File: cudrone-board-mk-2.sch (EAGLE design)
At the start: 1 part, among them U1 EDISON_CONNECTOR_FULLSOCKET

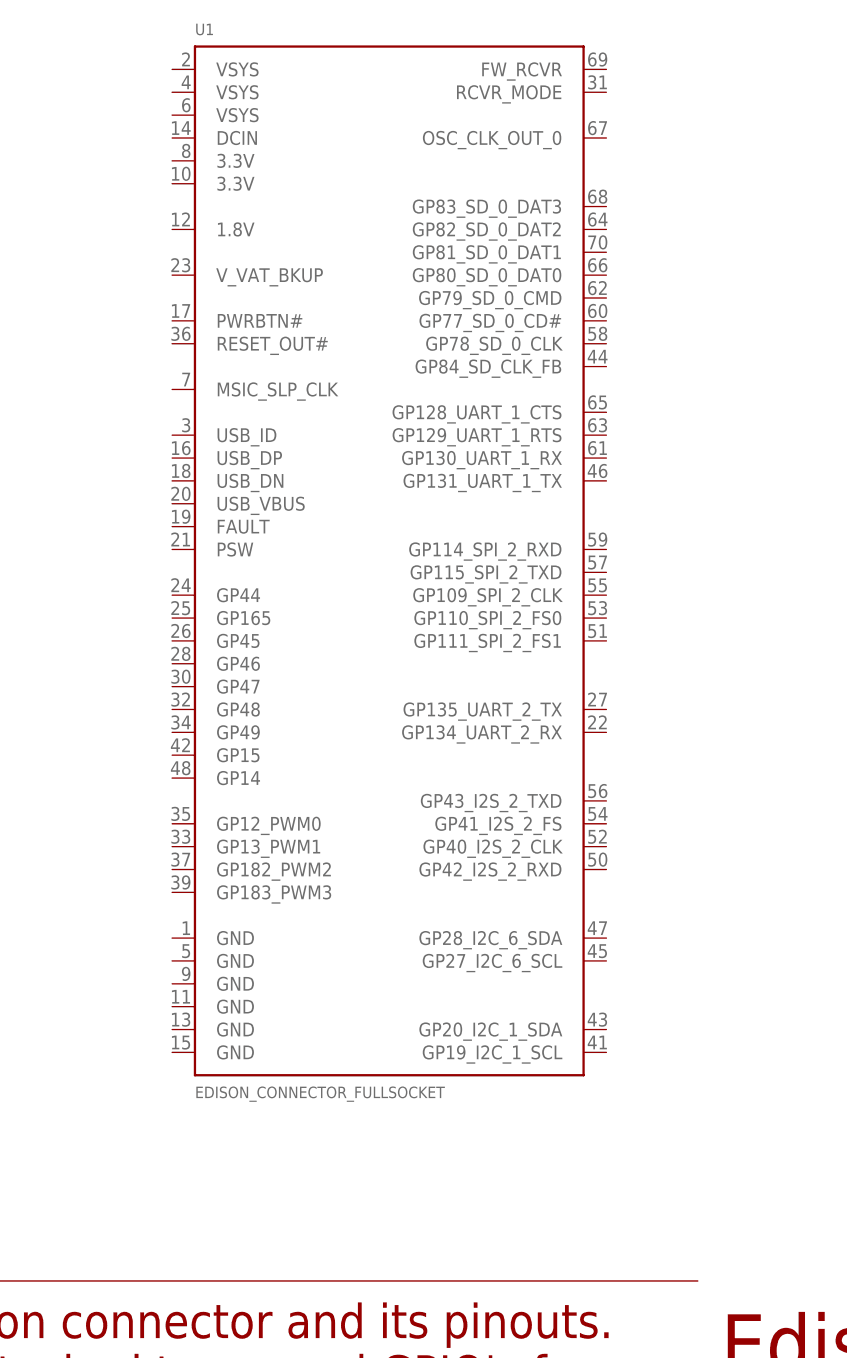
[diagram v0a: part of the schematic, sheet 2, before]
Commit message: Added several libraries
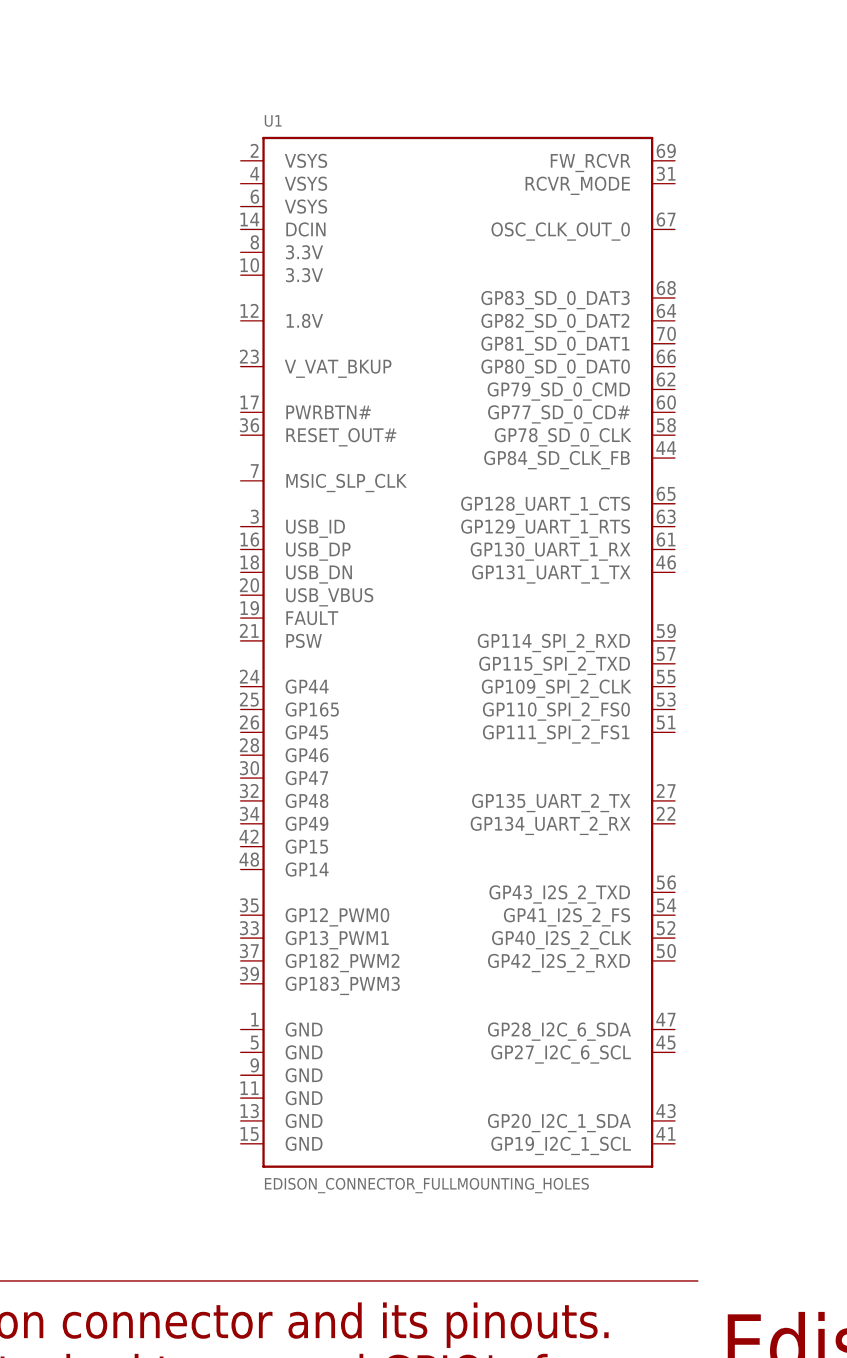
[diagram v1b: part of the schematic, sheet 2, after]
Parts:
- U1: value EDISON_CONNECTOR_FULLSOCKET -> EDISON_CONNECTOR_FULLMOUNTING_HOLES; device SparkFun-Boards:EDISON_CONNECTOR_FULLSOCKET -> SparkFun-Boards:EDISON_CONNECTOR_FULLMOUNTING_HOLES
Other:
- moved on the sheet: U1
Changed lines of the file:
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@@
 </classes>
 <parts>
-<part name="U1" library="SparkFun-Boards" deviceset="EDISON_CONNECTOR_FULL" device="SOCKET"/>
 <part name="FRAME1" library="frames" deviceset="LETTER_L" device=""/>
 <part name="FRAME2" library="frames" deviceset="LETTER_L" device=""/>
@@
 <part name="FRAME8" library="frames" deviceset="LETTER_L" device=""/>
 <part name="FRAME9" library="frames" deviceset="LETTER_L" device=""/>
+<part name="U1" library="SparkFun-Boards" deviceset="EDISON_CONNECTOR_FULL" device="MOUNTING_HOLES"/>
 </parts>
 <sheets>
@@
 </plain>
 <instances>
-<instance part="U1" gate="G$1" x="93.98" y="142.24"/>
 <instance part="FRAME1" gate="G$1" x="0" y="0"/>
 <instance part="FRAME1" gate="G$2" x="147.32" y="0"/>
+<instance part="U1" gate="G$1" x="101.6" y="132.08"/>
 </instances>
 <busses>

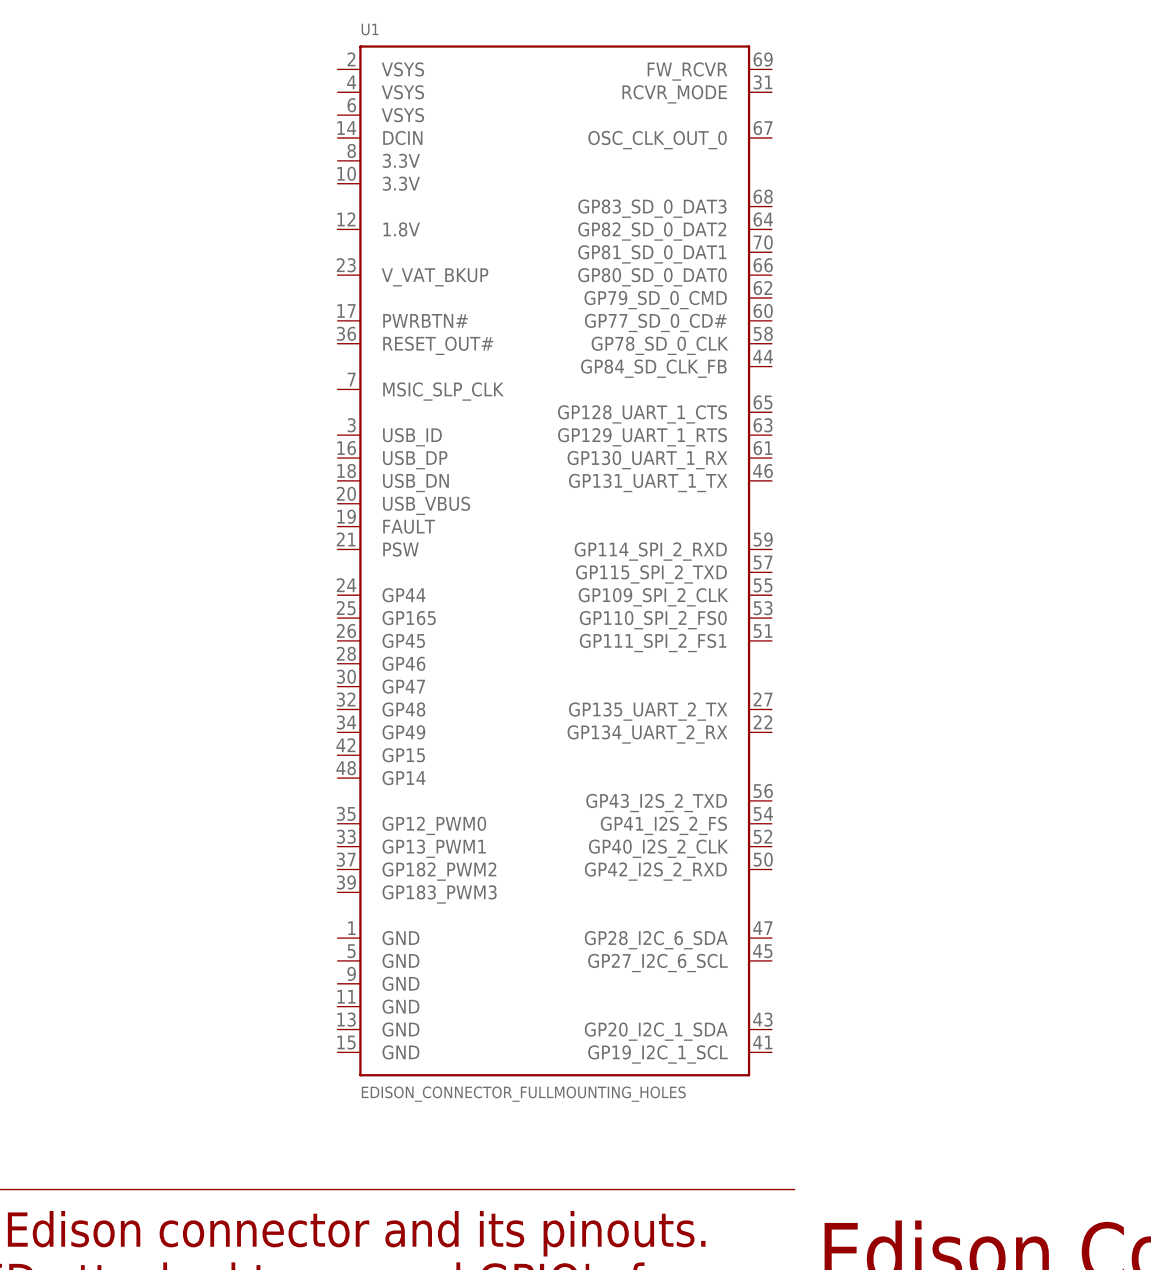
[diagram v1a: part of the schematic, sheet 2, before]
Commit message: Labeled edison nets and added RTC backup battery
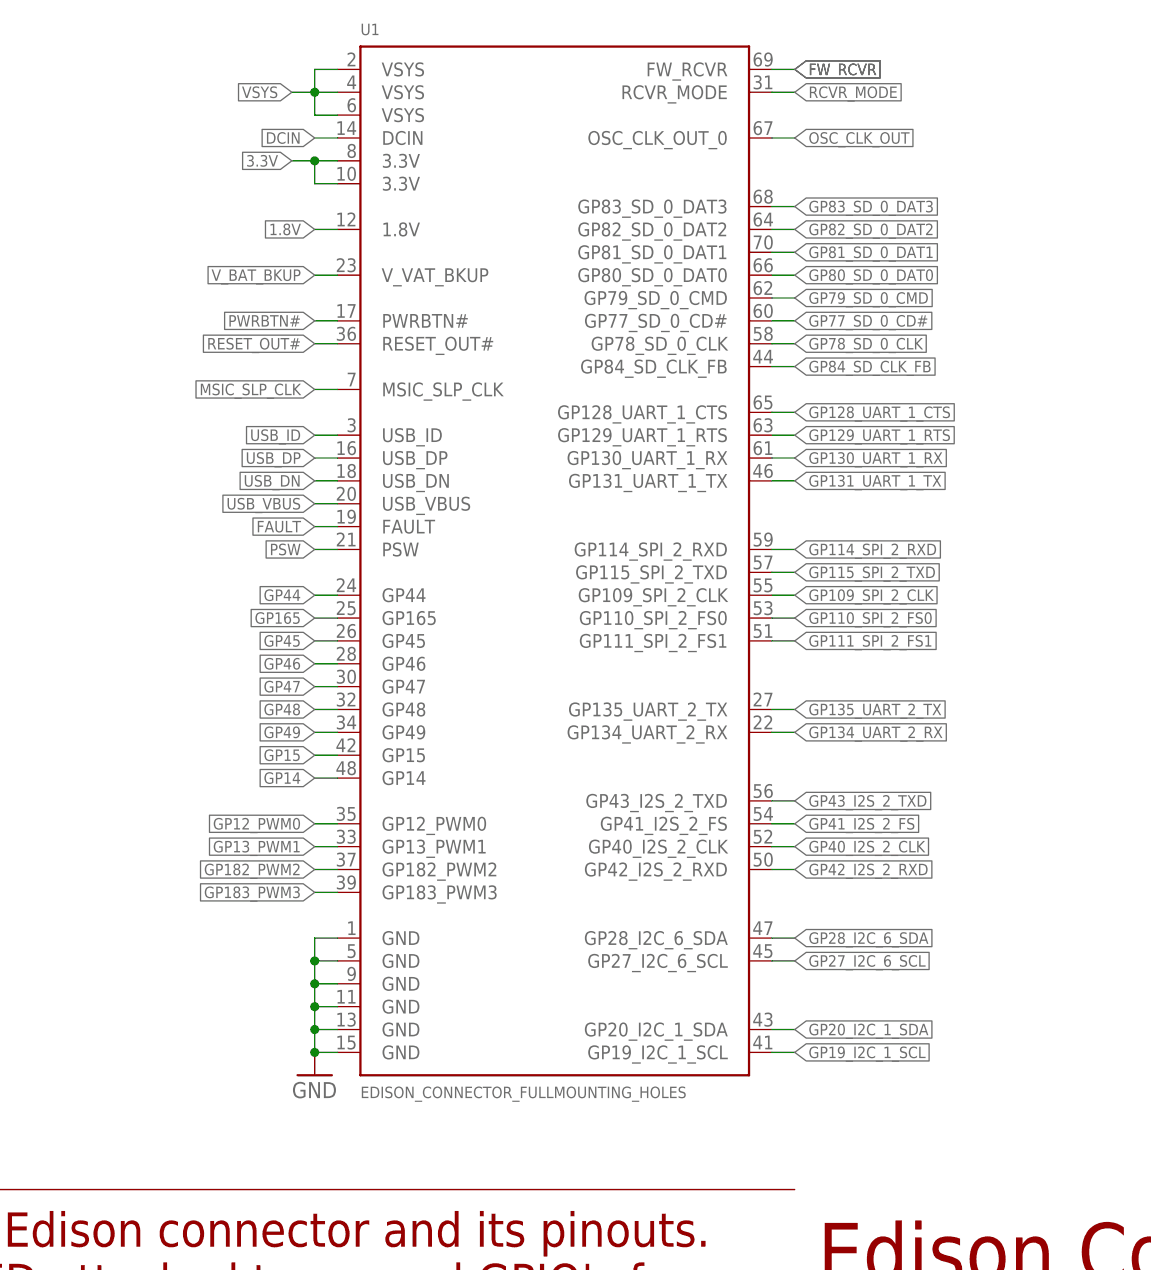
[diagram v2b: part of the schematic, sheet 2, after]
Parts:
- added BAT_BACKUP: RTC backup battery, SparkFun-Electromechanical:BATTERY12MM
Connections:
- new net 1.8V: U1.1.8V
- new net 3.3V: U1.3.3V@1, U1.3.3V@2
- new net DCIN: U1.DCIN
- new net FAULT: U1.FAULT
- new net FW_RCVR: U1.FW_RCVR
- new net GND: BAT_BACKUP.-, U1.GND@1, U1.GND@2, U1.GND@3, U1.GND@4, U1.GND@5, U1.GND@6
- new net GP109_SPI_2_CLK: U1.GP109_SPI_2_CLK
- new net GP110_SPI_2_FS0: U1.GP110_SPI_2_FS0
- new net GP111_SPI_2_FS1: U1.GP111_SPI_2_FS1
- new net GP114_SPI_2_RXD: U1.GP114_SPI_2_RXD
- new net GP115_SPI_2_TXD: U1.GP115_SPI_2_TXD
- new net GP128_UART_1_CTS: U1.GP128_UART_1_CTS
- new net GP129_UART_1_RTS: U1.GP129_UART_1_RTS
- new net GP12_PWM0: U1.GP12_PWM0
- new net GP130_UART_1_RX: U1.GP130_UART_1_RX
- new net GP131_UART_1_TX: U1.GP131_UART_1_TX
- new net GP134_UART_2_RX: U1.GP134_UART_2_RX
- new net GP135_UART_2_TX: U1.GP135_UART_2_TX
- new net GP13_PWM1: U1.GP13_PWM1
- new net GP14: U1.GP14
- new net GP15: U1.GP15
- new net GP165: U1.GP165
- new net GP182_PWM2: U1.GP182_PWM2
- new net GP183_PWM3: U1.GP183_PWM3
- new net GP19_I2C_1_SCL: U1.GP19_I2C_1_SCL
- new net GP20_I2C_1_SDA: U1.GP20_I2C_1_SDA
- new net GP27_I2C_6_SCL: U1.GP27_I2C_6_SCL
- new net GP28_I2C_6_SDA: U1.GP28_I2C_6_SDA
- new net GP40_I2S_2_CLK: U1.GP40_I2S_2_CLK
- new net GP41_I2S_2_FS: U1.GP41_I2S_2_FS
- new net GP42_I2S_2_RXD: U1.GP42_I2S_2_RXD
- new net GP43_I2S_2_TXD: U1.GP43_I2S_2_TXD
- new net GP44: U1.GP44
- new net GP45: U1.GP45
- new net GP46: U1.GP46
- new net GP47: U1.GP47
- new net GP48: U1.GP48
- new net GP49: U1.GP49
- new net GP77_SD_0_CD#: U1.GP77_SD_0_CD#
- new net GP78_SD_0_CLK: U1.GP78_SD_0_CLK
- new net GP79_SD_0_CMD: U1.GP79_SD_0_CMD
- new net GP80_SD_0_DAT0: U1.GP80_SD_0_DAT0
- new net GP81_SD_0_DAT1: U1.GP81_SD_0_DAT1
- new net GP82_SD_0_DAT2: U1.GP82_SD_0_DAT2
- new net GP83_SD_0_DAT3: U1.GP83_SD_0_DAT3
- new net GP84_SD_CLK_FB: U1.GP84_SD_CLK_FB
- new net MSIC_SLP_CLK: U1.MSIC_SLP_CLK
- new net OSC_CLK_OUT: U1.OSC_CLK_OUT_0
- new net PSW: U1.PSW
- new net PWRBTN#: U1.PWRBTN#
- new net RCVR_MODE: U1.RCVR_MODE
- new net RESET_OUT#: U1.RESET_OUT#
- new net USB_DN: U1.USB_DN
- new net USB_DP: U1.USB_DP
- new net USB_ID: U1.USB_ID
- new net USB_VBUS: U1.USB_VBUS
- new net VSYS: U1.VSYS@1, U1.VSYS@2, U1.VSYS@3
- new net V_BAT_BKUP: BAT_BACKUP.+, U1.V_VAT_BKUP
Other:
- note added: "Contains switching power regulator and RTC backup battery."
- note removed: "This sheet provides the power for main bus from esc power It contains a backup battery chargerwhich automatically kicks in the battery if the main power fails and signals the main controller so it can take action. It also contains nessisary regulators. There are also LED status lights. Contains power moniter which communicates via I2C"

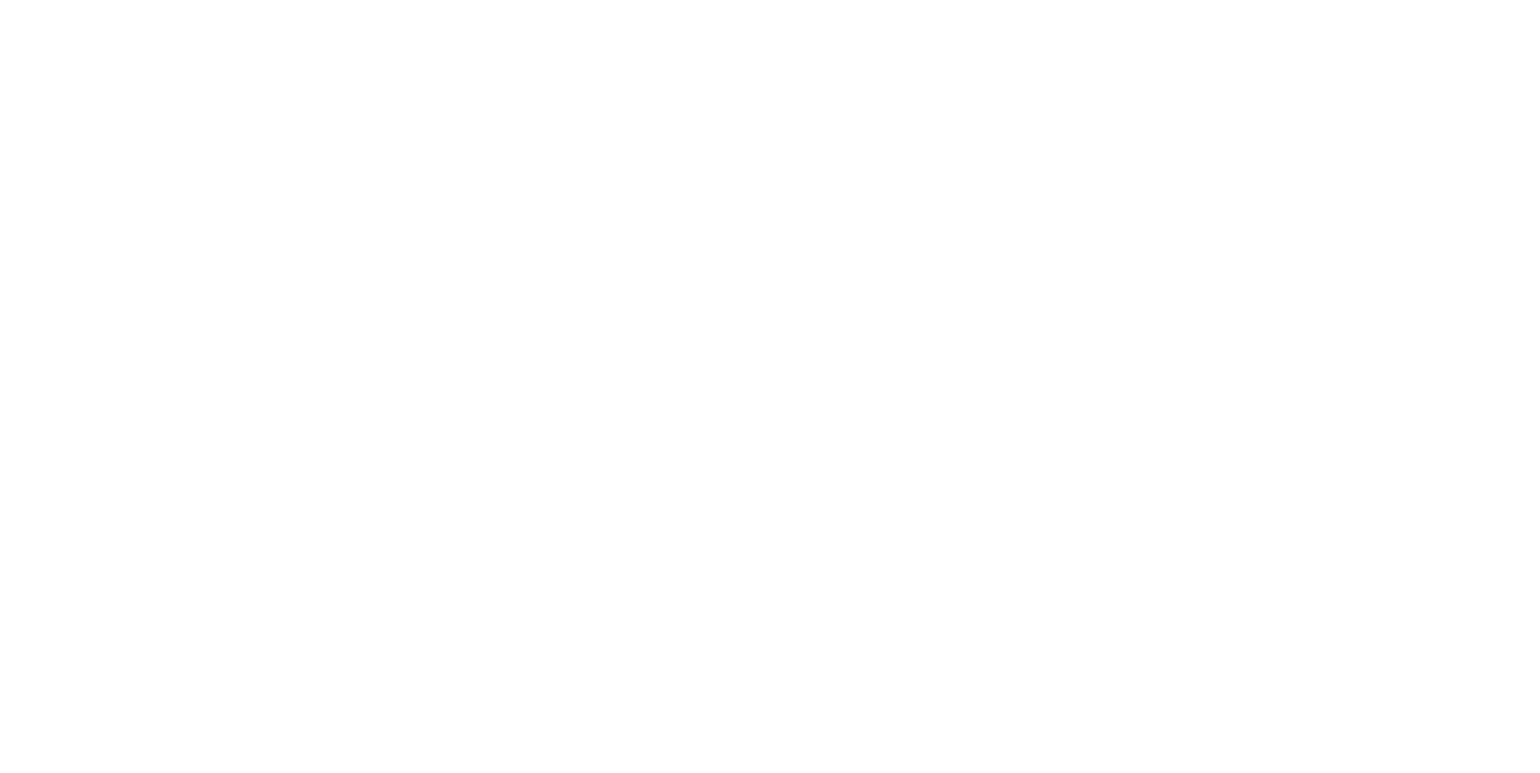
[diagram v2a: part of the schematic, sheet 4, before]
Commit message: Added contents of base block to schematic
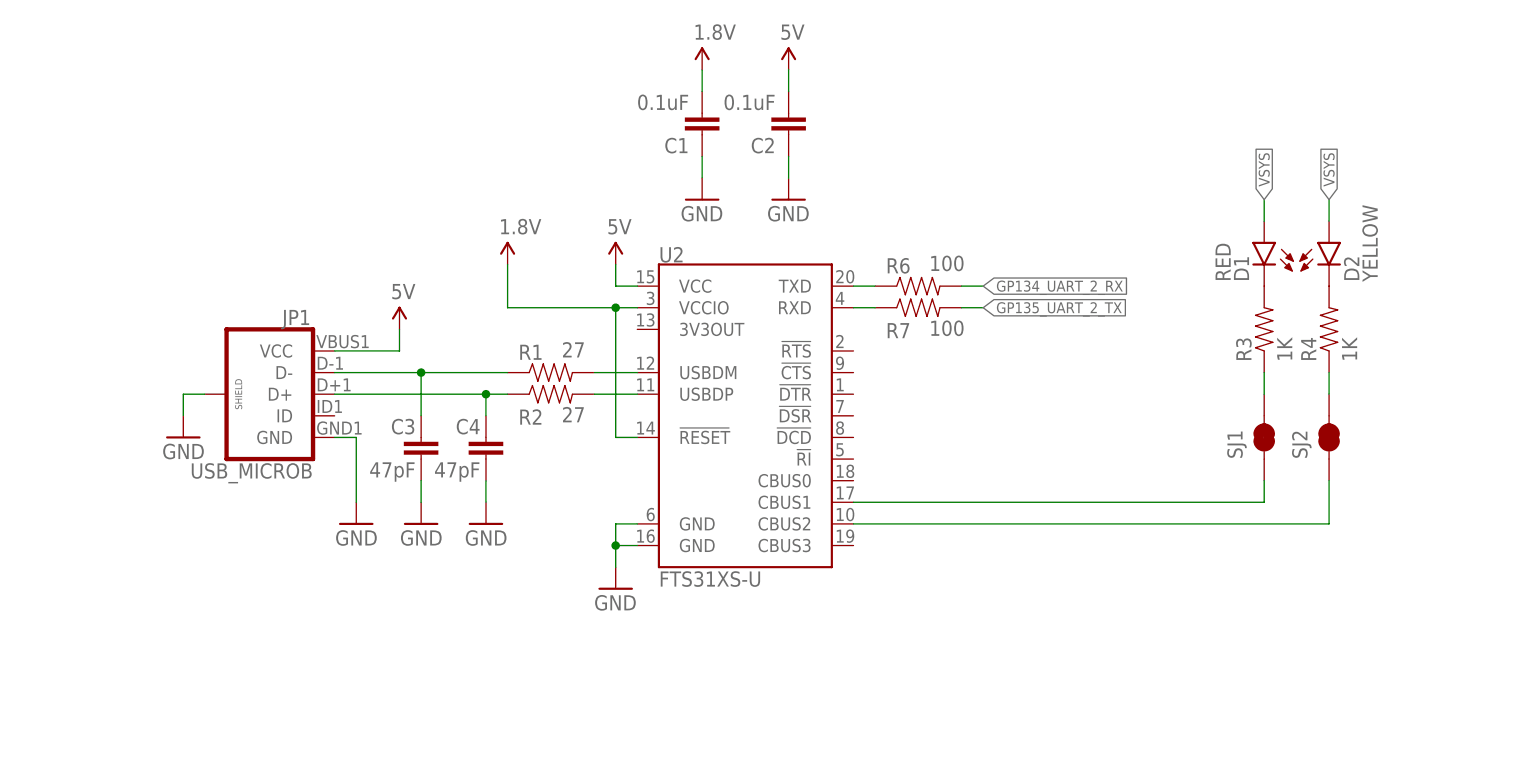
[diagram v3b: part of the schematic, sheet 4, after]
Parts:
- added C1, C2: 0.1uF, SparkFun-Capacitors:0.1UF-25V(+80/-20%)(0603)
- added C3, C4, C7: 47pF, SparkFun-Capacitors:47PF-50V-5%(0603)
- added C6, C9: 22uF, SparkFun-Capacitors:22UF-6.3V-20%(0805)
- added C8: 10uF, SparkFun-Capacitors:10UF-6.3V-20%(1206)
- added D1: RED, SparkFun-LED:LED-RED0603
- added D2: YELLOW, SparkFun-LED:LED-YELLOW0603
- added D3: BLUE, SparkFun-LED:LED-BLUE0603
- added D4: DIODE-SCHOTTKY-MBRA140, SparkFun-DiscreteSemi:DIODE-SCHOTTKY-MBRA140
- added JP1: USB_MICROB, SparkFun-Connectors:USB_MICROB_PLUGCONN-11752
- added L1: 1.0uH, SparkFun-Passives:INDUCTOR
- added Q1: BSS138, SparkFun-DiscreteSemi:MOSFET-NCHANNELBSS138
- added R1, R2: 27, SparkFun-Resistors:27OHM1/10W1%(0603)
- added R10: 287, SparkFun-Resistors:287OHM-1/10W-1%(0603)
- added R11, R8: 10K, SparkFun-Resistors:10KOHM1/10W1%(0603)0603
- added R12: 100k, SparkFun-Resistors:100KOHM1/10W1%(0603)
- added R13: 680k, SparkFun-Resistors:RESISTOR0603
- added R14: 120k, SparkFun-Resistors:RESISTOR0603
- added R15, R3, R4, R5: 1K, SparkFun-Resistors:1KOHM1/10W1%(0603)
- added R6, R7: 100, SparkFun-Resistors:100OHM1/10W1%(0603)
- added R9: 220, SparkFun-Resistors:22OHM1/10W1%(0603)
- added S1: POWER, SparkFun-Electromechanical:SWITCH-MOMENTARY-2TACTILE-SWITCH-SMD-RIGHT-ANGLE
- added SJ1, SJ2, SJ3: JUMPER-PAD-2-NC_BY_TRACE, SparkFun-Passives:JUMPER-PAD-2-NC_BY_TRACE
- added U$3: MIC2039, Testing:MIC2039
- added U2: FTS31XS-U, SparkFun-DigitalIC:FT231XS
- added U3: (no value), SparkFun-Connectors:USB-ABCONN-11794
- added U4: TPS62065, Testing:TPS62065
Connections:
- new net 5V: C2.2, C9.1, D4.C, JP1.VCC, R15.2, U$3.VIN, U2.VCC, U4.AVIN, U4.EN, U4.PVIN
- new net N$1: SJ1.1, U2.CBUS1
- new net N$10: D2.C, R4.2
- new net N$11: R6.1, U2.TXD
- new net N$12: D3.C, R5.2
- new net N$13: R5.1, SJ3.2
- new net N$14: R7.1, U2.RXD
- new net N$15: R8.2, R9.2, S1.1
- new net N$16: R10.2, U$3.ILIM
- new net N$17: C7.2, R13.1, R14.2, U4.FB
- new net N$18: Q1.G, R15.1
- new net N$19: L1.1, U4.SW
- new net N$2: C3.1, JP1.D-, R1.1
- new net N$3: C4.1, JP1.D+, R2.1
- new net N$4: R1.2, U2.USBDM
- new net N$5: R2.2, U2.USBDP
- new net N$6: SJ2.1, U2.CBUS2
- new net N$7: R3.1, SJ1.2
- new net N$8: R4.1, SJ2.2
- new net N$9: D1.C, R3.2
- net 1.8V: now also C1.2, R11.1, U2.!RESET, U2.VCCIO
- net DCIN: now also Q1.S
- net FAULT: now also R11.2, U$3.!FAULT
- net GND: now also C1.1, C2.1, C3.2, C4.2, C6.2, C8.2, C9.2, JP1.GND, JP1.SHIELD, R10.1, R12.1, R14.1, S1.2, SJ3.1, U$3.GND, U2.GND@16, U2.GND@6, U3.GND, U4.AGND, U4.PAD, U4.PG, U4.PGND
- net GP134_UART_2_RX: now also R6.2
- net GP135_UART_2_TX: now also R7.2
- net PSW: now also R12.2, U$3.EN
- net PWRBTN#: now also R9.1
- net USB_DN: now also U3.D-
- net USB_DP: now also U3.D+
- net USB_ID: now also U3.USBID
- net USB_VBUS: now also C8.1, D4.A, U$3.VOUT, U3.VBUS
- net VSYS: now also C6.1, C7.1, D1.A, D2.A, D3.A, L1.2, Q1.D, R13.2, R8.1
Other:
- note added: "DCIN Enable Circuit Prevents Battery board from enabling DCIN"
